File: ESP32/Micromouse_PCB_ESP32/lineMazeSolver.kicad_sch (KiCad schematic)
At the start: 26 parts, among them J1 Power_supply, J2 Conn_01x11_Pin, J3 Motor_Left, J4 Motor_Right, SW1 SW_SPST, SW2 SW_Push, SW3 SW_Push, SW4 SW_Push, U1 AMS1117-5.0, U2 DM-OLED096-636, U3 ESP32-DEVKIT-V1

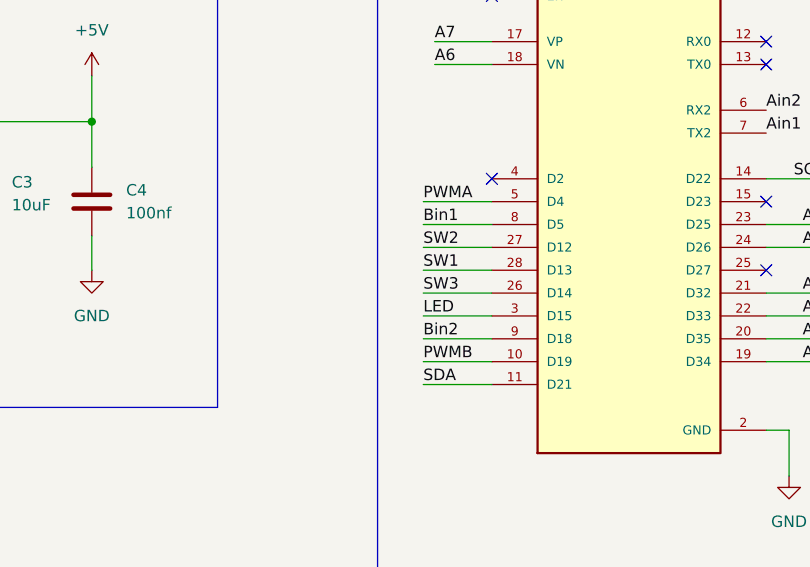
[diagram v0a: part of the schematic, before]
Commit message: Added a new features with NANO Based pcb PCB
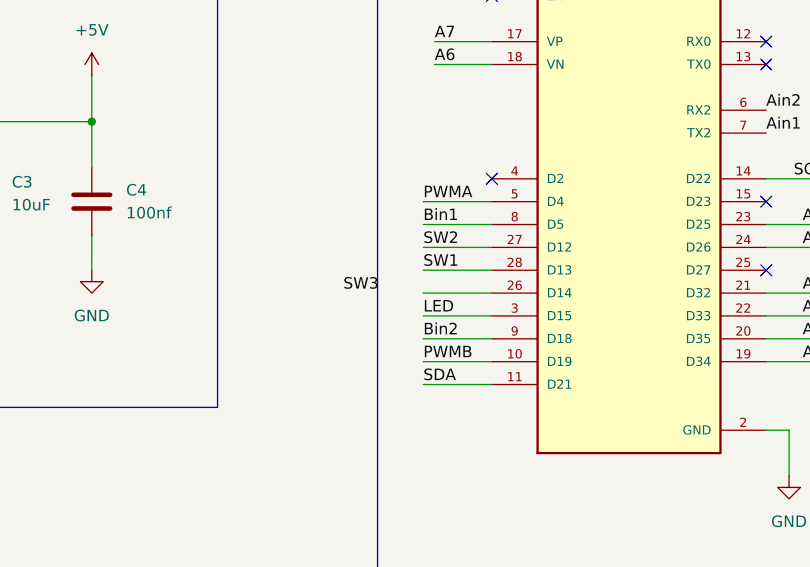
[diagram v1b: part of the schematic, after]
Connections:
- net SW3: no longer U3.26 (D14)
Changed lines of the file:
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@@
 	)
 	(label "SW3"
-		(at 124.46 67.31 0)
+		(at 115.57 67.31 0)
 		(effects
 			(font

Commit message: Added PCB Design for Arduino nano
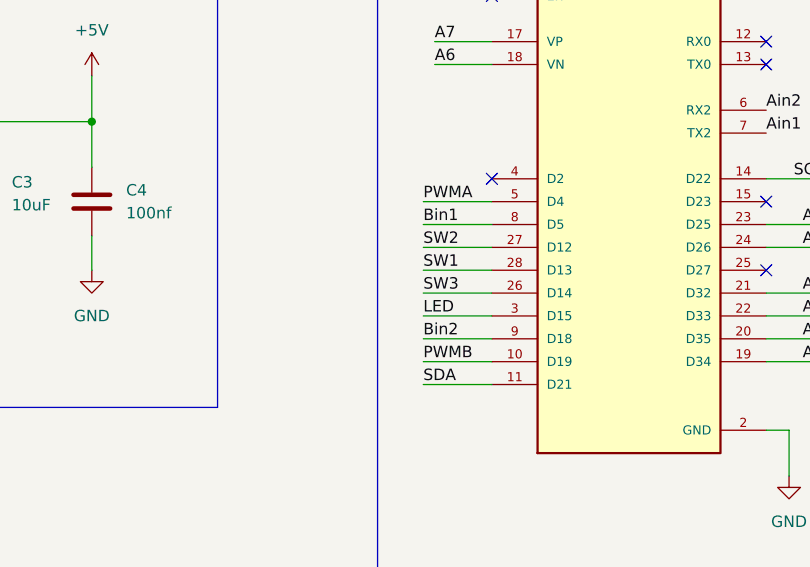
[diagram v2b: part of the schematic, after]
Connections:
- net SW3: now also U3.26 (D14)
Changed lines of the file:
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@@
 	)
 	(label "SW3"
-		(at 115.57 67.31 0)
+		(at 124.46 67.31 0)
 		(effects
 			(font
